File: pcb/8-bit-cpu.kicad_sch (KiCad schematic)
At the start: 16 parts, among them J1 Conn_01x24_Socket, J2 Conn_01x24_Socket, SW1 CLK MODE, SW2 CLK PULSE, SW3 BOOTLOAD EN, SW4 RAM MODE, SW5 RAM PULSE, U1 Tang Nano, U2 CA56-12EWA

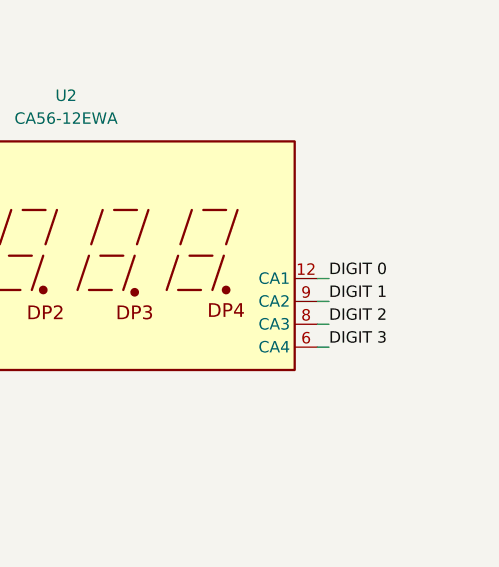
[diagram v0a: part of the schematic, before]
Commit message: Added current limiting resistors to display
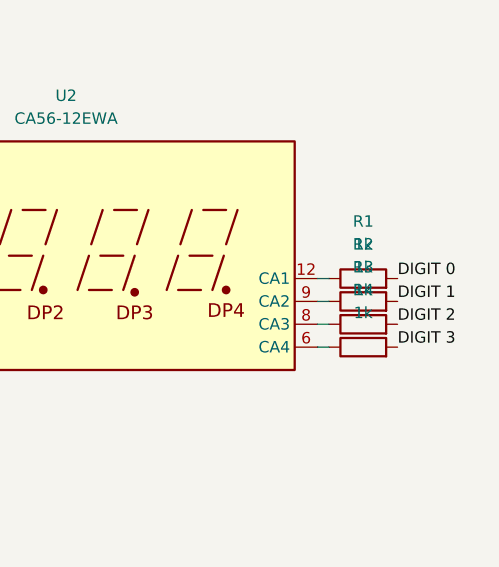
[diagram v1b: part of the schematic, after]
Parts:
- added R1, R2, R3, R4: 1k, Resistor_THT:R_Axial_DIN0309_L9.0mm_D3.2mm_P12.70mm_Horizontal, symbol Device:R
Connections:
- net DIGIT 0: now also R1.2; no longer U2.12 (CA1)
- net DIGIT 1: now also R2.2; no longer U2.9 (CA2)
- net DIGIT 2: now also R3.2; no longer U2.8 (CA3)
- net DIGIT 3: now also R4.2; no longer U2.6 (CA4)
- new net: R1.1, U2.12 (CA1)
- new net: R4.1, U2.6 (CA4)
- new net: R3.1, U2.8 (CA3)
- new net: R2.1, U2.9 (CA2)
